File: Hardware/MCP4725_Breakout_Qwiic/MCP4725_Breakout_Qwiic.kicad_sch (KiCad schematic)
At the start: 17 parts, among them J1 Conn_01x02, J2 I2C, U2 MCP4725

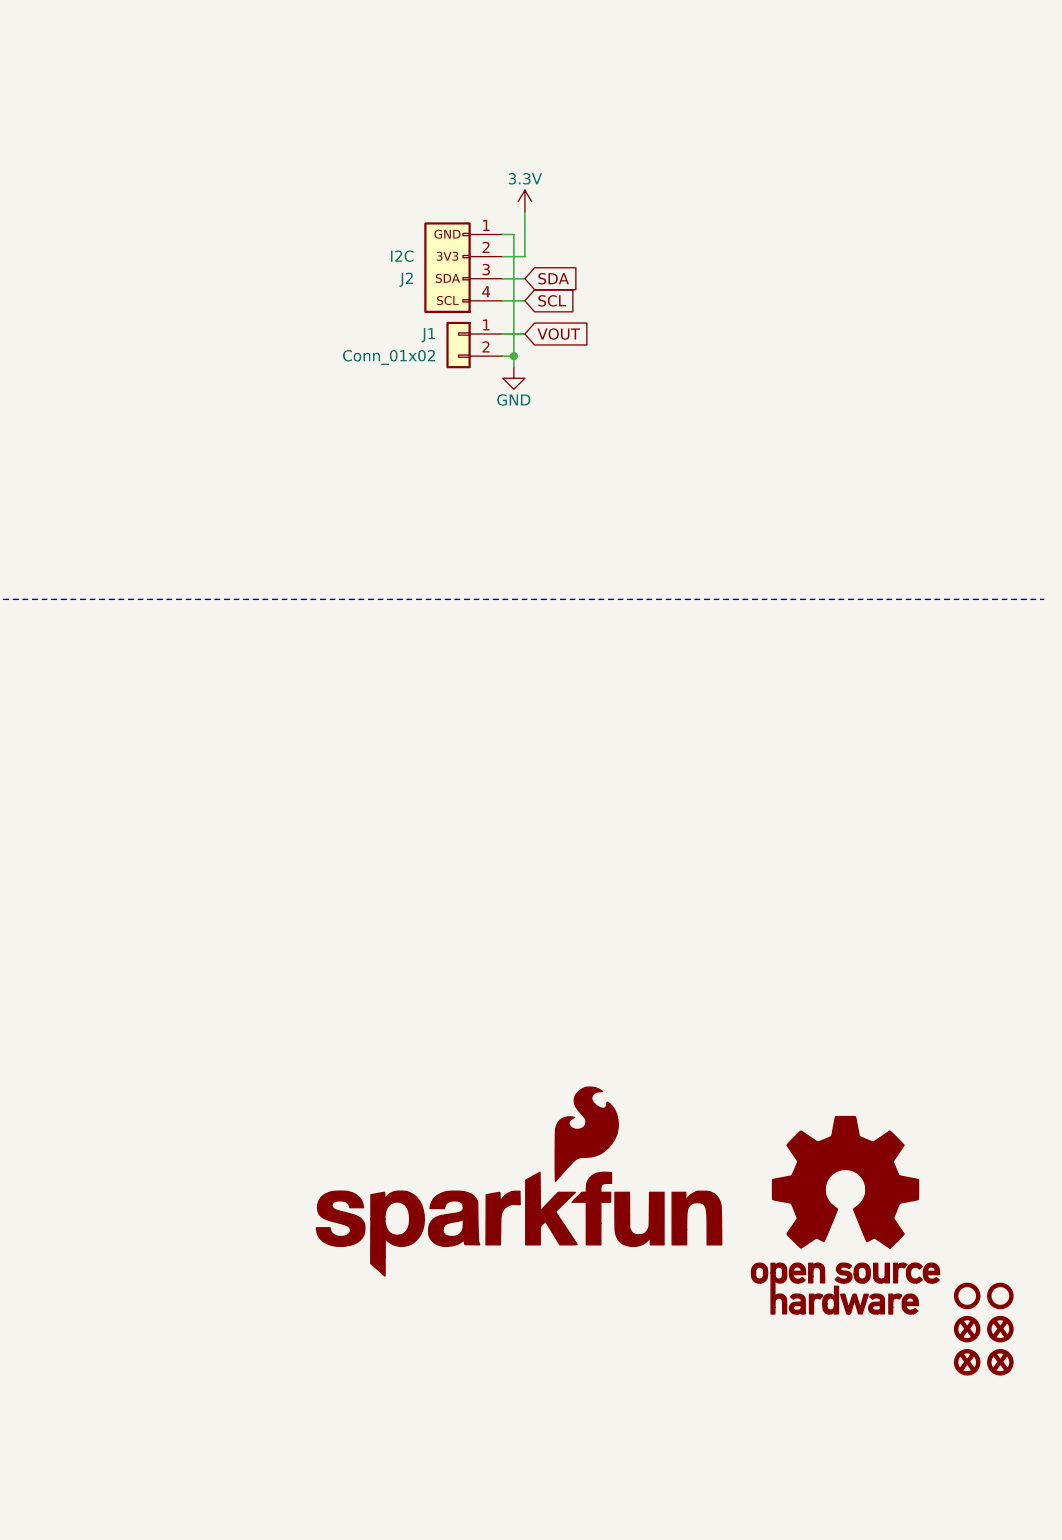
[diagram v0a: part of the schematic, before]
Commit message: Routes Qwiic Board, adds
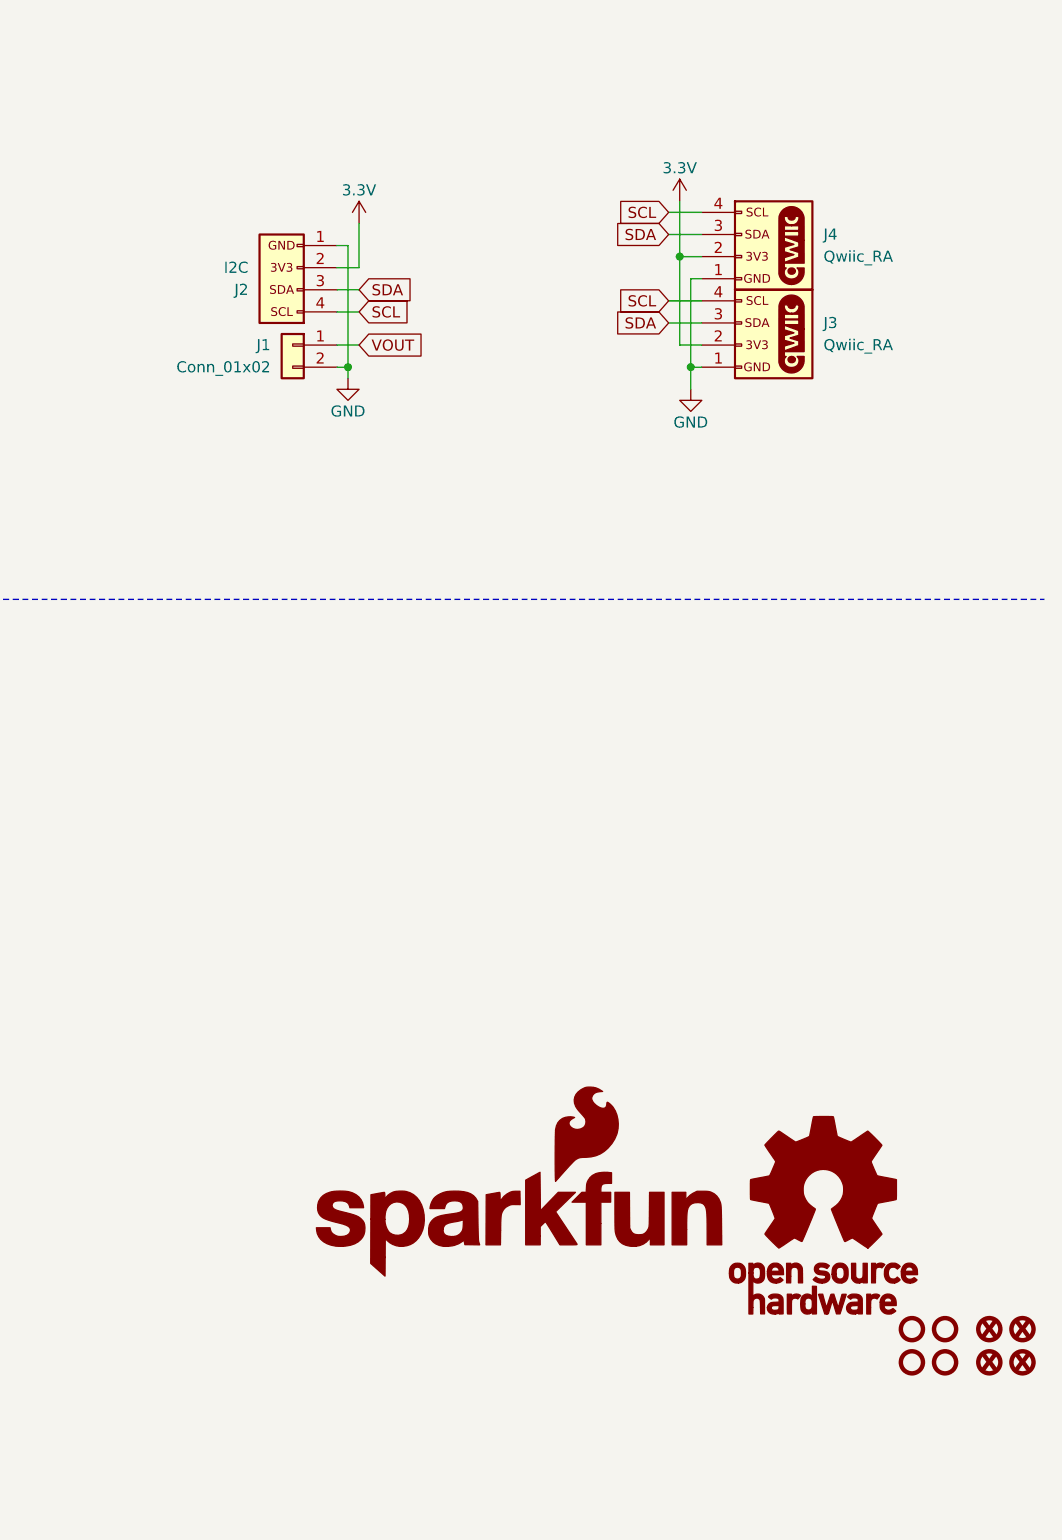
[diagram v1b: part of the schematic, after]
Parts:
- added J3, J4: Qwiic_RA, SparkFun-Connector:JST_1x04_P1.0mm_Horizontal_SMD, symbol SparkFun-Connector:Qwiic_Horizontal
- added ST3, ST4: Standoff, SparkFun-Hardware:Standoff, symbol SparkFun-Hardware:Standoff
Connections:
- net 3.3V: now also J3.2 (Pin_2), J4.2 (Pin_2)
- net GND: now also J3.1 (Pin_1), J4.1 (Pin_1)
- net SCL: now also J3.4 (Pin_4), J4.4 (Pin_4)
- net SDA: now also J3.3 (Pin_3), J4.3 (Pin_3)
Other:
- moved on the sheet: J1, J2

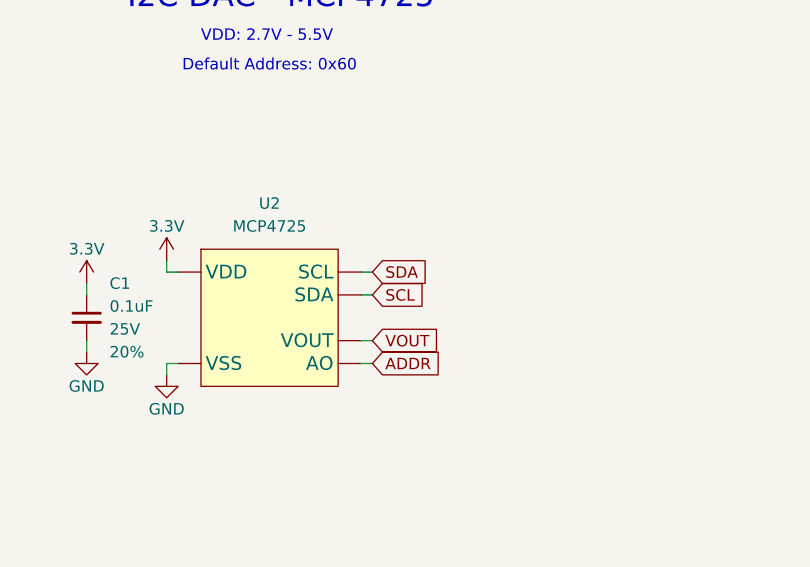
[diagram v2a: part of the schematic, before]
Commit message: Fixes swapped pins on SCL/SDA
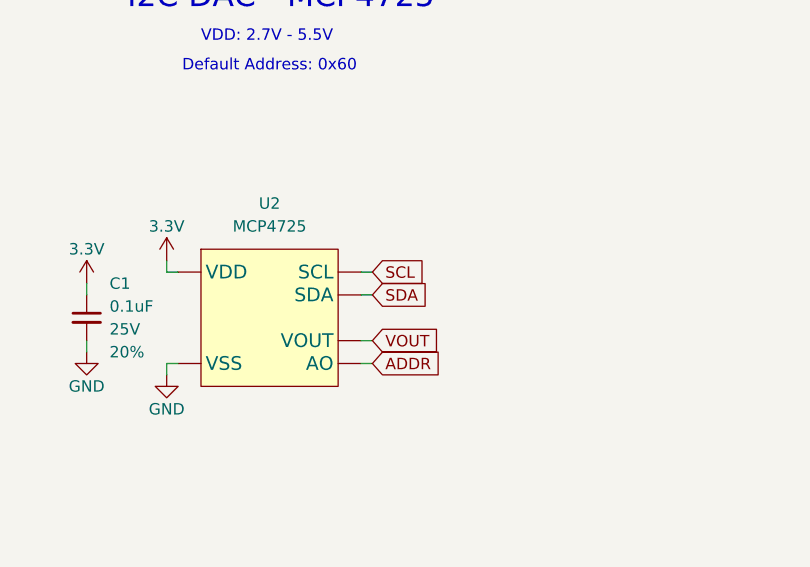
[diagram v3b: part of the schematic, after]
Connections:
- net SCL: now also U2.5 (SCL); no longer U2.4 (SDA)
- net SDA: now also U2.4 (SDA); no longer U2.5 (SCL)

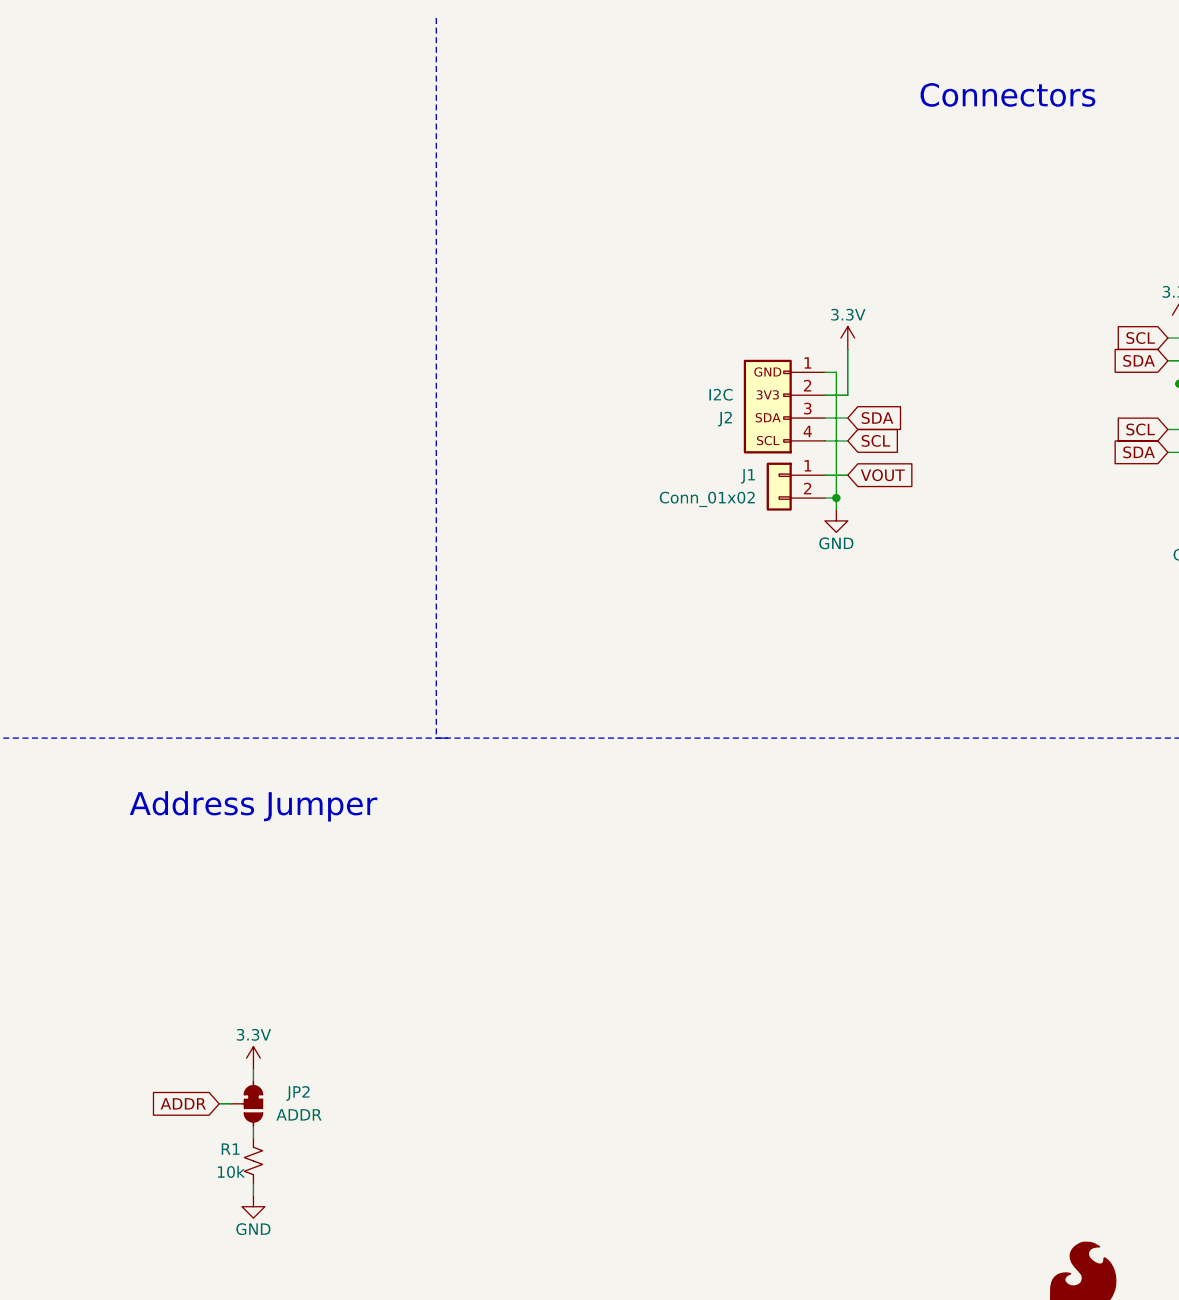
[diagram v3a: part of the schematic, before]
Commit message: Adds Qwiic Logo, power LED, adds "DAC" to product silk
* Fixes the address jumper
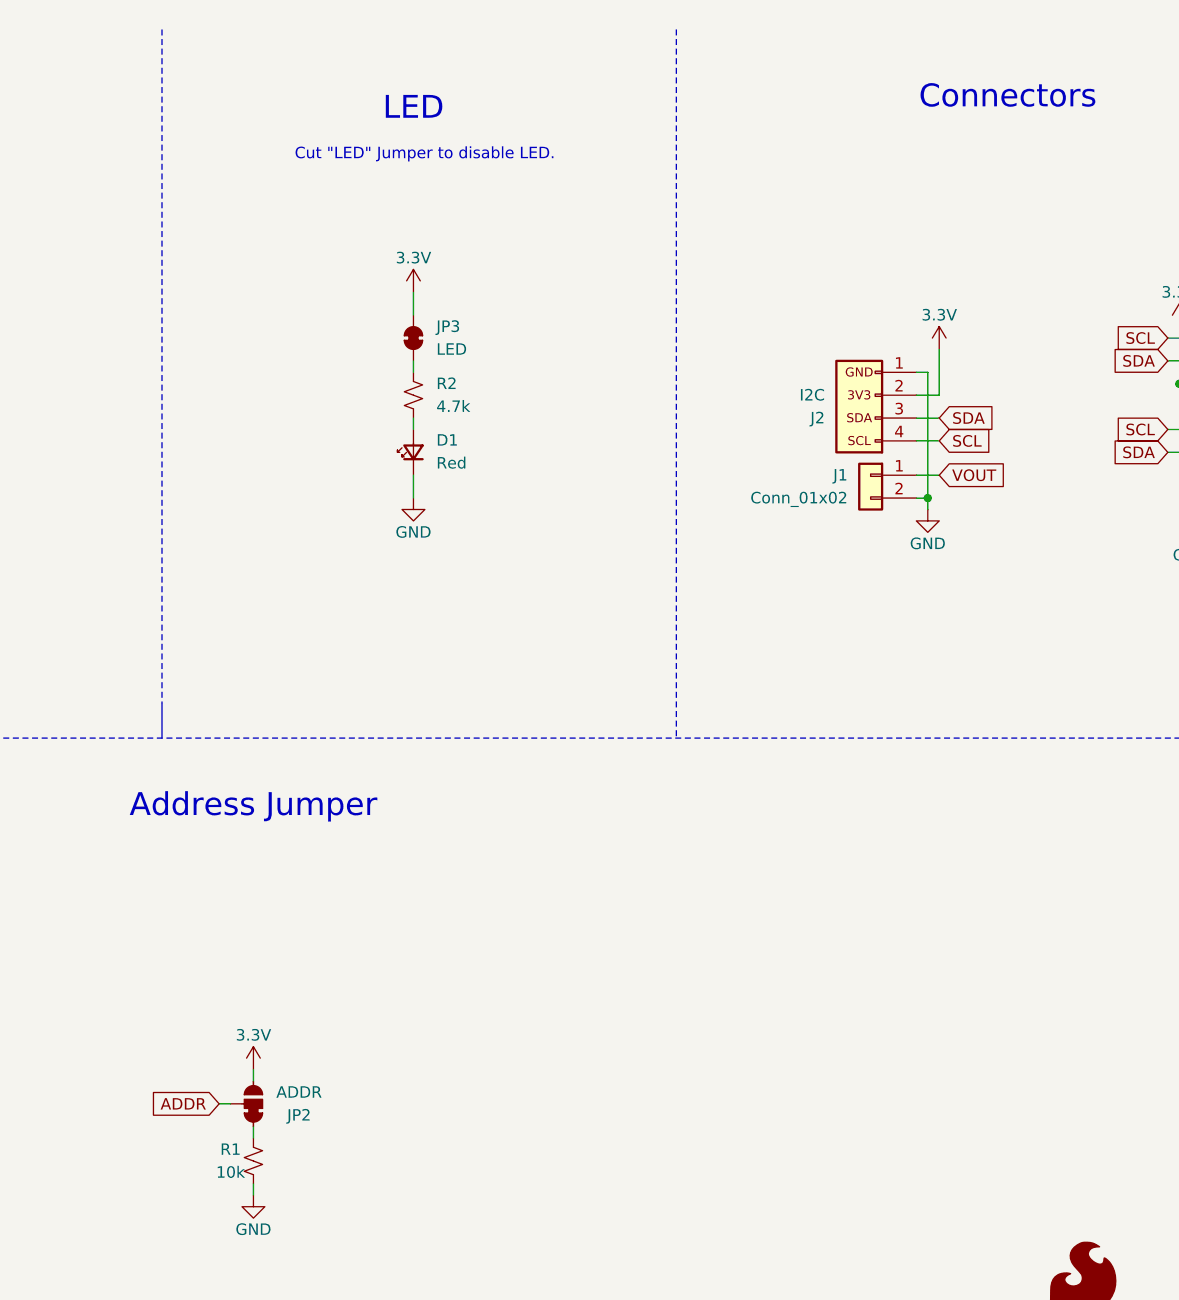
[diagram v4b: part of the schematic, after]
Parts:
- added D1: Red, SparkFun-LED:LED_0603_1608Metric_Red, symbol SparkFun-LED:LED_Red_0603
- added JP3: LED, SparkFun-Jumper:Jumper_2_NC_Trace, symbol SparkFun-Jumper:SolderJumper_2_Bridged
- added R2: 4.7k, SparkFun-Resistor:R_0603_1608Metric, symbol SparkFun-Resistor:4.7k_0603
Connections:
- net 3.3V: now also JP2.3 (C), JP3.2 (B); no longer JP2.1 (A)
- net GND: now also D1.1 (K)
- net at R1.2: now also JP2.1 (A); no longer JP2.3 (C)
- new net: D1.2 (A), R2.1
- new net: JP3.1 (A), R2.2
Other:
- note added: "Cut "LED" Jumper to disable LED."
- note added: "LED"
- title: SparkFun I2C DAC - MCP4725 -> SparkFun I2C DAC - MCP4725 (Qwiic)
- moved on the sheet: J1, J2
